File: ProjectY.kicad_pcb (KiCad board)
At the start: 6 copper layers, 100 x 70 mm, 286 parts, among them IC2 R7KA8P1KFLCAB#UC0, J1 UI Board Connector, J17 Out, J2 Conn_ARM_JTAG_SWD_10, J3 9V, J5 IN_R, J6 IN_L, J7 Out, J9 USB_C_Receptacle_USB2.0_14P, K1 G6K-2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

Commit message: layout is almost finished
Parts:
- removed C1, C2, C30, C38, C44, C58, C8, C9: 4.7uF, PCM_JLCPCB:C_0402
- removed C12, C13, C25, C46: 10uF, PCM_JLCPCB:C_0402
- removed C27: 100nF, PCM_JLCPCB:C_0402
- removed Q1: AO3401A, PCM_JLCPCB:Q_SOT-23
- removed R24: 100Ω, PCM_JLCPCB:R_0603
- C106, C107, C31, C401, C97, C98, R23, R25, R26, R27, R28, R48: moved to F.Cu
- TP10, TP5, TP6, TP9: moved to B.Cu
- moved C57 50.6 mm to (211.1, 132.9), turned to -90 degrees
- moved TP5 44.0 mm to (180.1, 159.6)
- moved TP6 41.4 mm to (173.3, 157.2)
- moved TP10 40.7 mm to (176.0, 155.9)
- moved TP8 38.6 mm to (170.8, 156.1)
- moved TP9 38.1 mm to (179.7, 162.2)
- moved TP7 33.0 mm to (170.8, 162.0)
- moved C34 12.4 mm to (175.8, 149.8), turned to -90 degrees
- moved L7 10.8 mm to (180.4, 150.1), turned to 0 degrees
- moved C51 10.4 mm to (173.5, 149.8), turned to -90 degrees
- moved C32 9.78 mm to (169.9, 150.9), turned to 0 degrees
- moved C96 9.44 mm to (188.0, 162.8)
- moved C33 8.98 mm to (169.9, 153.3), turned to 0 degrees
- moved C26 5.23 mm to (183.0, 154.9), turned to -90 degrees
- moved L6 5.15 mm to (190.0, 156.8)
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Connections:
- C26 pad 1: Net-(Q1-D) -> +3.3V
- C28 pad 1: Net-(Q1-D) -> +3.3V
- C29 pad 1: Net-(Q1-D) -> +3.3V
- C89 pad 1: Net-(Q1-D) -> +3.3V
- L6 pad 1: Net-(Q1-D) -> +3.3V
- U17 pad 10: Net-(U17-ENN) -> +3.3V
- U17 pad 4: Net-(U17-ENN) -> +3.3V
- U17 pad 7: Net-(Q1-G) -> unconnected-(U17-BSW-Pad7)
- U17 pad 8: Net-(U17-ENN) -> +3.3V
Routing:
- net /Analog Audio/GP0: track 0.01 -> 48.1 mm, vias 1 -> 2
- net Net-(R36-Pad1): track 1.74 -> 39.9 mm, vias 0 -> 1
- net /DSP/JTAG_TDO: track 1.11 -> 36.2 mm, vias 1 -> 2
- net /DSP/~{RESET}: track 0.76 -> 32.8 mm, vias 1 -> 2
- net /DSP/JTAG_TDI: track 0.76 -> 32.0 mm, vias 1 -> 2
- net /DSP/JTAG_TCK: track 1.77 -> 29.9 mm, vias 1 -> 2
- net Net-(Q3-B): track 0.03 -> 27.8 mm, vias 1 -> 2
- net /DSP/JTAG_TMS: track 0.48 -> 27.3 mm, vias 1 -> 2
- net GND: track 64.0 -> 88.9 mm, vias 178 -> 225
- net AGND: track 157.7 -> 180.4 mm, vias 15 -> 16
- net +7V: track 0.00 -> 18.2 mm, vias 1 -> 0
- net +3.3V: track 31.1 -> 48.0 mm, vias 69 -> 74
- net Net-(Q1-G): track 14.6 -> 0.00 mm
- net /Analog Audio/I2S_CK: track 28.6 -> 42.5 mm
- net -7V: track 0.32 -> 12.4 mm, vias 1 -> 0
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- removed copper zone on F.Cu, net Net-(Q1-D)

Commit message: 0 airwires finally
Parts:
- C57: moved to F.Cu
- moved C57 4.49 mm to (207.2, 135.3), turned to 0 degrees
- moved C14 0.30 mm to (227.1, 105.2)
- moved L7 0.10 mm to (180.4, 150.0)
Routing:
- net GND: track 88.9 -> 98.2 mm, vias 225 -> 231
- net ISO_GND: track 0.00 -> 9.18 mm, vias 0 -> 15
- net /DSP/JTAG_TMS: track 27.3 -> 36.1 mm
- net Net-(U202A--): track 1.59 -> 9.23 mm, vias 0 -> 2
- net /DSP/JTAG_TCK: track 29.9 -> 37.1 mm
- net /DSP/VBUS: track 0.00 -> 5.48 mm, vias 0 -> 4
- net +3.3V: track 48.0 -> 53.1 mm
- net /DSP/D_iso-: track 9.58 -> 14.1 mm
- net /DSP/JTAG_TDI: track 32.0 -> 36.3 mm
- net /DSP/CC: track 0.00 -> 3.10 mm
- net /DSP/D_iso+: track 9.83 -> 12.8 mm
- net /DSP/VCONN: track 0.00 -> 2.89 mm
- net /DSP/UD-: track 0.00 -> 2.88 mm
- net /DSP/UD+: track 0.00 -> 2.85 mm
- net AGND: track 180.4 -> 183.2 mm
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- added copper zone on B.Cu, net +3.3V
- added copper zone on In4.Cu, net /DSP/VBUS
- added copper zone on In4.Cu, net GND
- added copper zone on In1.Cu, net ISO_GND
- removed copper zone on In4.Cu, net +3.3V

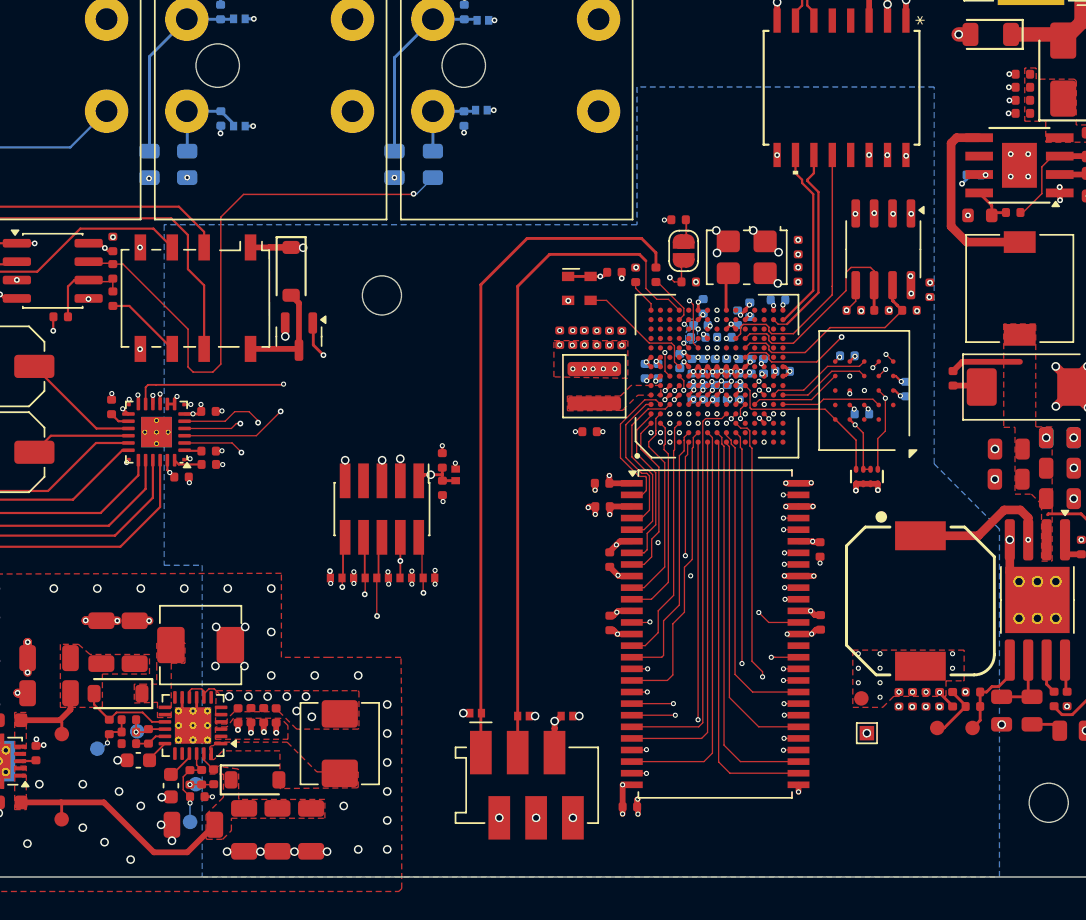
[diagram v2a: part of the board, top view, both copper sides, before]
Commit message: RAM routing was fixed
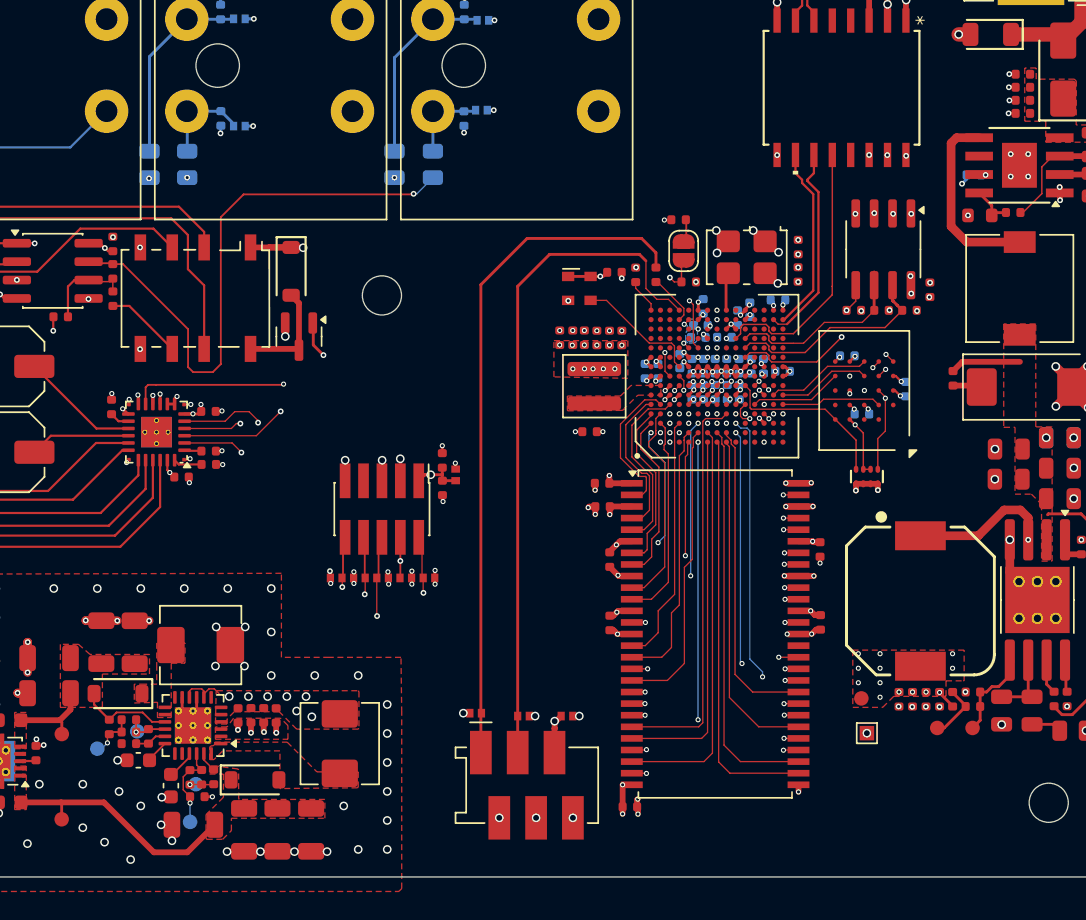
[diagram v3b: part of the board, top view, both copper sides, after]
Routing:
- net /DSP/FRAM_SCL: track 15.2 -> 13.1 mm
- net /DSP/RAM_A11: track 23.3 -> 23.9 mm
- net /DSP/RAM_BA0: track 24.9 -> 24.8 mm, vias 2 -> 3
- net /DSP/RAM_BA1: track 28.7 -> 28.6 mm, vias 2 -> 3
- net /DSP/RAM_CKE: vias 2 -> 3
- added copper zone on In4.Cu, net +3.3V
- removed copper zone on B.Cu, net +3.3V
- removed copper zone on In4.Cu, net GND
